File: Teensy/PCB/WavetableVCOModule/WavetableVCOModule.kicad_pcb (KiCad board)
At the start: 2 copper layers, 55.9 x 101.6 mm, 32 parts, among them J1 Micro_SD_Card, SW1 Next_File_Button, U1 SPI_Oled, U2 Teensy4.0

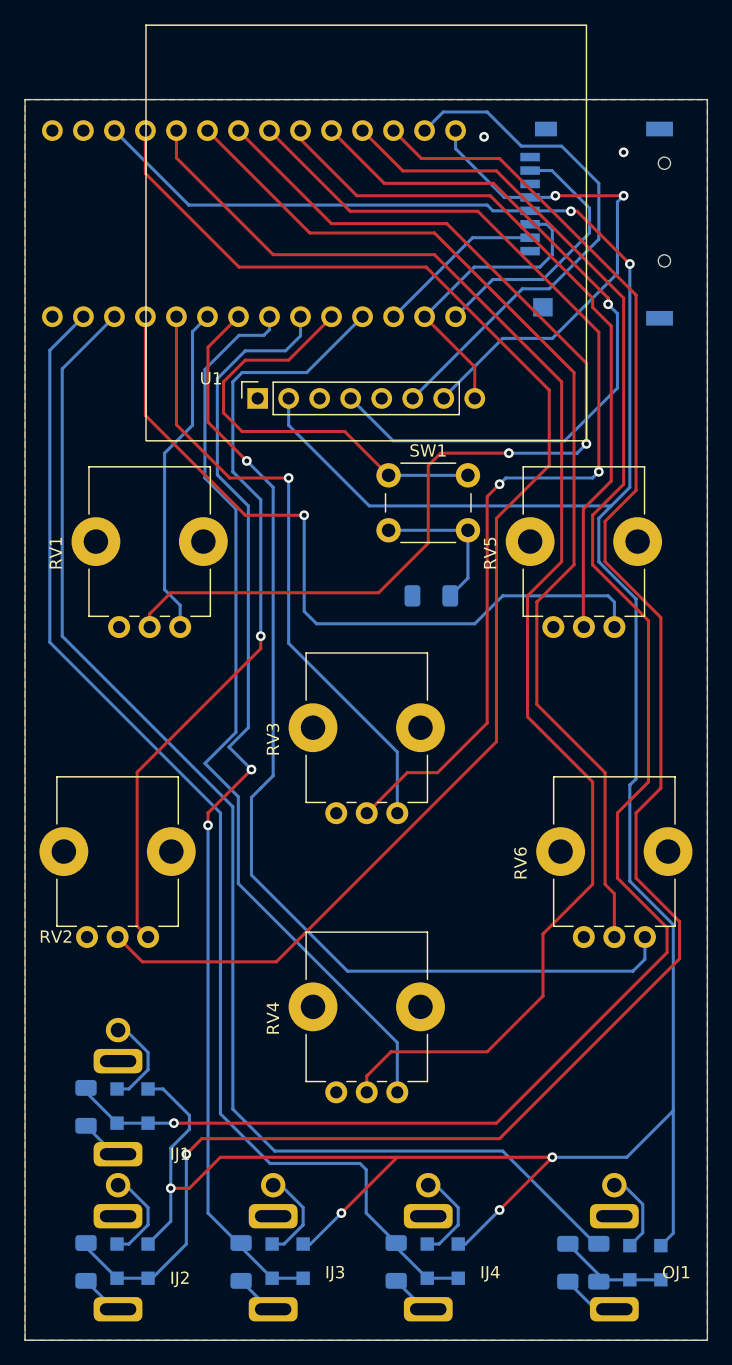
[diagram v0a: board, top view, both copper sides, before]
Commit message: Added Power connector and bracket
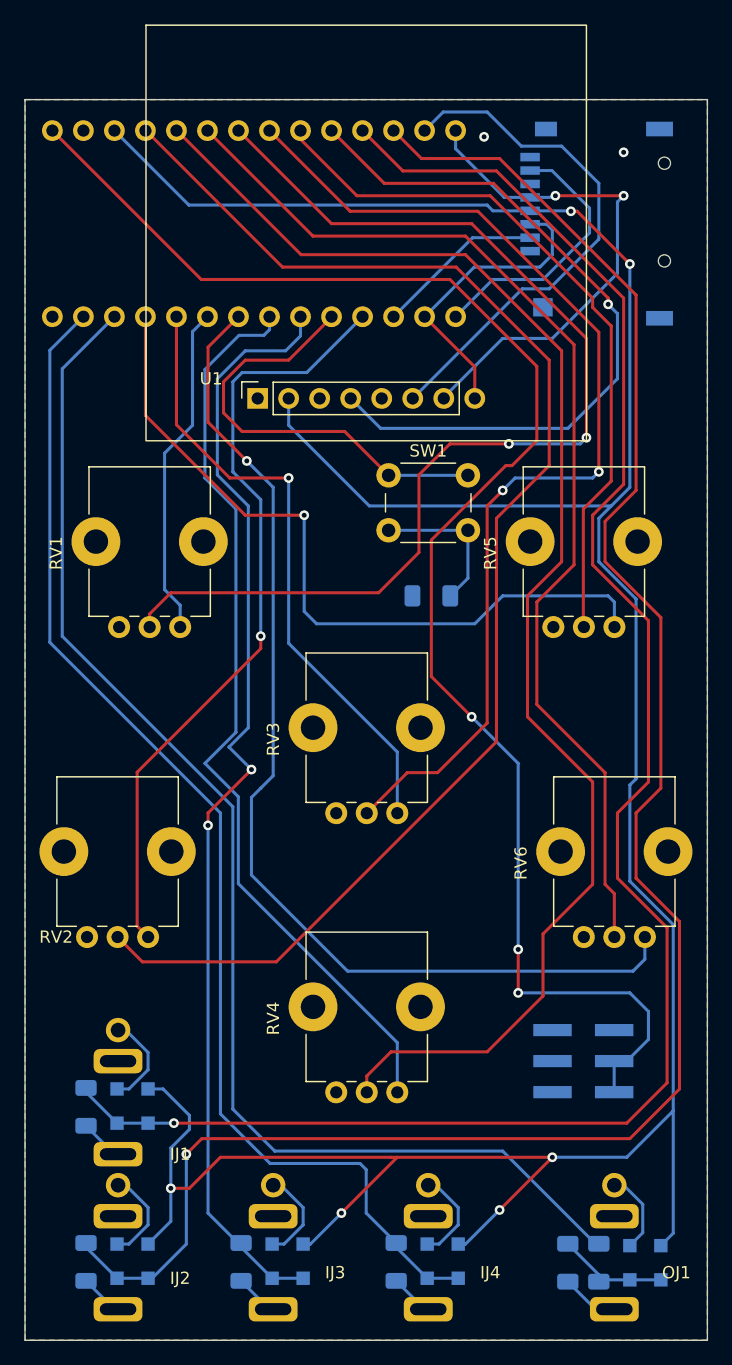
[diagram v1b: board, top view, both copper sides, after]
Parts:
- added J2: Power_Connector_2x3, Connector_PinHeader_2.54mm:PinHeader_2x03_P2.54mm_Vertical_SMD, B.Cu at (109.2, 149.9)
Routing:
- net +5V: track 0.00 -> 125.5 mm, vias 0 -> 3
- net /T16: track 141.1 -> 147.4 mm
- net /T15: track 150.2 -> 156.4 mm
- net /T21: track 88.3 -> 89.7 mm
- net /T17: track 61.1 -> 59.8 mm
- net /T20: track 89.3 -> 90.2 mm
- net /T23: track 113.8 -> 113.2 mm
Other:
- board text added: "+"
